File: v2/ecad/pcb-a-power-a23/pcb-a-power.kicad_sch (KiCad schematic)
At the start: 392 parts, among them Q1 2N7002: panel controller high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, Q10 CSD18510Q5B 40 V N-FET, Q11 CSD18510Q5B 40 V N-FET, Q12 CSD18510Q5B 40 V N-FET, Q13 CSD18510Q5B 40 V N-FET, Q14 CSD18510Q5B 40 V N-FET, Q15 CSD18510Q5B 40 V N-FET, Q16 CSD18510Q5B 40 V N-FET, Q17 CSD19532Q5B 100 V N-FET (4.6 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, Q18 CSD19532Q5B 100 V N-FET (4.6 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, Q19 CSD19532Q5B 100 V N-FET (4.6 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, Q2 CSD19532Q5B 100 V N-FET (4.6 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, Q20 CSD19532Q5B 100 V N-FET (4.6 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, Q21 CSD18510Q5B 40 V N-FET, Q22 CSD18510Q5B 40 V N-FET, Q23 CSD18510Q5B 40 V N-FET, Q24 CSD18510Q5B 40 V N-FET, Q25 CSD18510Q5B 40 V N-FET, Q26 CSD18510Q5B 40 V N-FET, Q27 CSD18510Q5B 40 V N-FET (VBUS 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, Q3 CSD19532Q5B 100 V N-FET (4.6 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, Q4 CSD19532Q5B 100 V N-FET (4.6 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, Q5 CSD19532Q5B 100 V N-FET (4.6 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, Q6 2N7002: CHG_INHIBIT high = IL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, Q7 CSD18510Q5B 40 V N-FET, Q8 CSD18510Q5B 40 V N-FET, Q9 CSD18510Q5B 40 V N-FET, U1 LTC2954CTS8-1 push-button on/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, U10 INA226 rail monitor +5V_S3, U11 INA226 rail monitor +5V_DEV, U12 TPS62933DRLR 3 A buck, 3.3 V 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, U13 LM5176PWPR buck-boost control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, U14 INA226 PA rail monitor (0x46), U15 LM5176PWPR buck-boost control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, U16 LM5176PWPR buck-boost control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, U17 INA226 PoE rail monitor (0x47), U18 TPS25740ARGER USB-C PD source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, U19 LM5176PWPR buck-boost control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, U2 LM5176PWPR buck-boost control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, U21 TPS259631DDAR eFuse VBAT -> V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, U22 TPS259631DDAR eFuse VBAT -> V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, U23 TPS259631DDAR eFuse +5V_DEV -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, U26 SN74LVC08APWR quad AND: EMCON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, U27 PCA9555PW (0x21): enables and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, U28 PCA9555PW (0x24): power-good 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, U29 USBLC6-2SC6, U3 BQ25731RSNR 1 to 5 cell buck-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, U4 AP64500SP-13 5 A buck, 5.1 V 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, U5 AP64500SP-13 5 A buck, 5.1 V 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, U6 AP64500SP-13 5 A buck, 5.1 V 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, U7 AP64500SP-13 5 A buck, 5.1 V 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, U8 INA226 rail monitor +5V_S1, U9 INA226 rail monitor +5V_S2

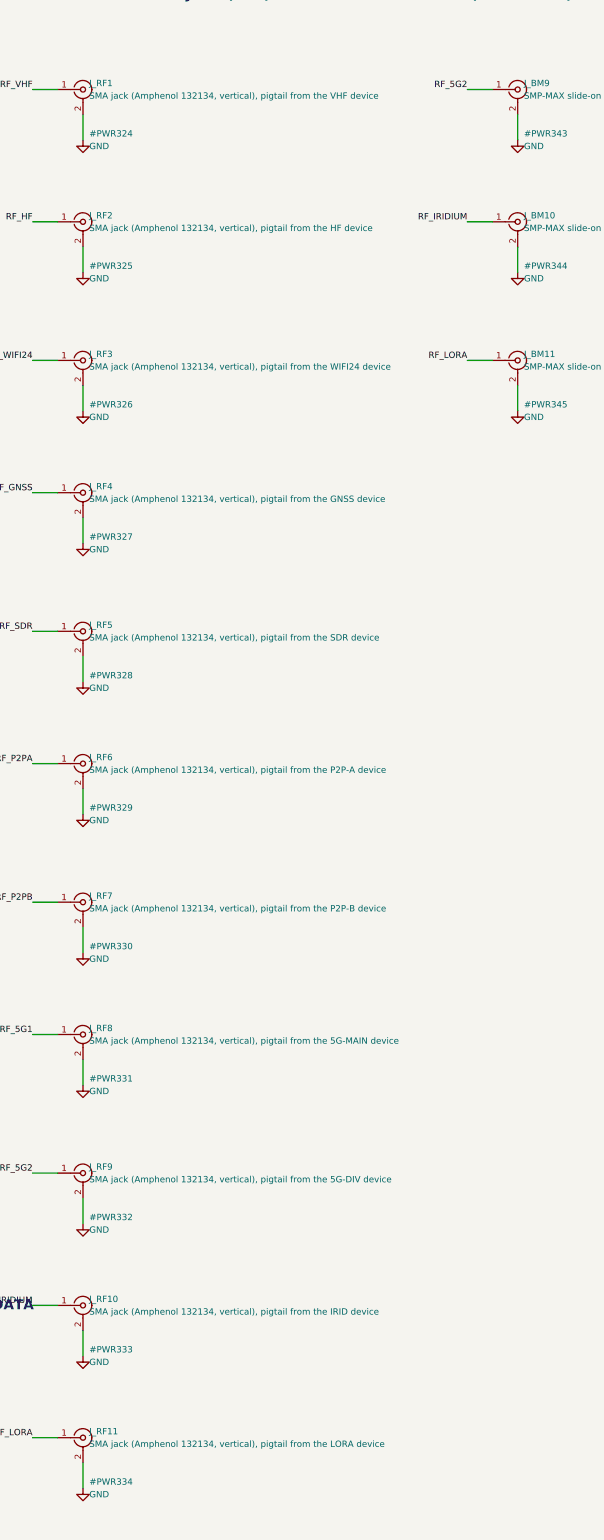
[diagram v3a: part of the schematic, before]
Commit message: feat(pcb-a,pcb-e): A24 re-cut and E7 cut, and boards A and E certify PASS [MESHSAT-862]
E7: routeflow ended CLEAN. hard 0, unrouted 0, check_pcb_e 88 of 88, dc_drop 2 of 2 rails MET,
netlist_board 816 of 816 with 18 aliased pins, verify_deliverable ALL PASS on 35 of 35, board sha256
b54cec80 matching the deliverable's own record. It carries today's connector corrections: the JST-VH
inlet and panel rows on C274411, the XT60-M pack connector on C98733, and the LT8705A's QFN order code
in place of the TSSOP one.

A24 re-cut with the SMA rows naming the jack instead of the radio at the far end of the pigtail. Same
board, same copper, one more text pass.

jlc_certify on the two of them: 223 components, 194 CERTIFIED, 23 HAND_FIT each with a written purchase
route, 6 BENCH_FITTED, NOTHING OPEN. It is the first PASS the certifier has returned on any board since
it was written on 11 September.
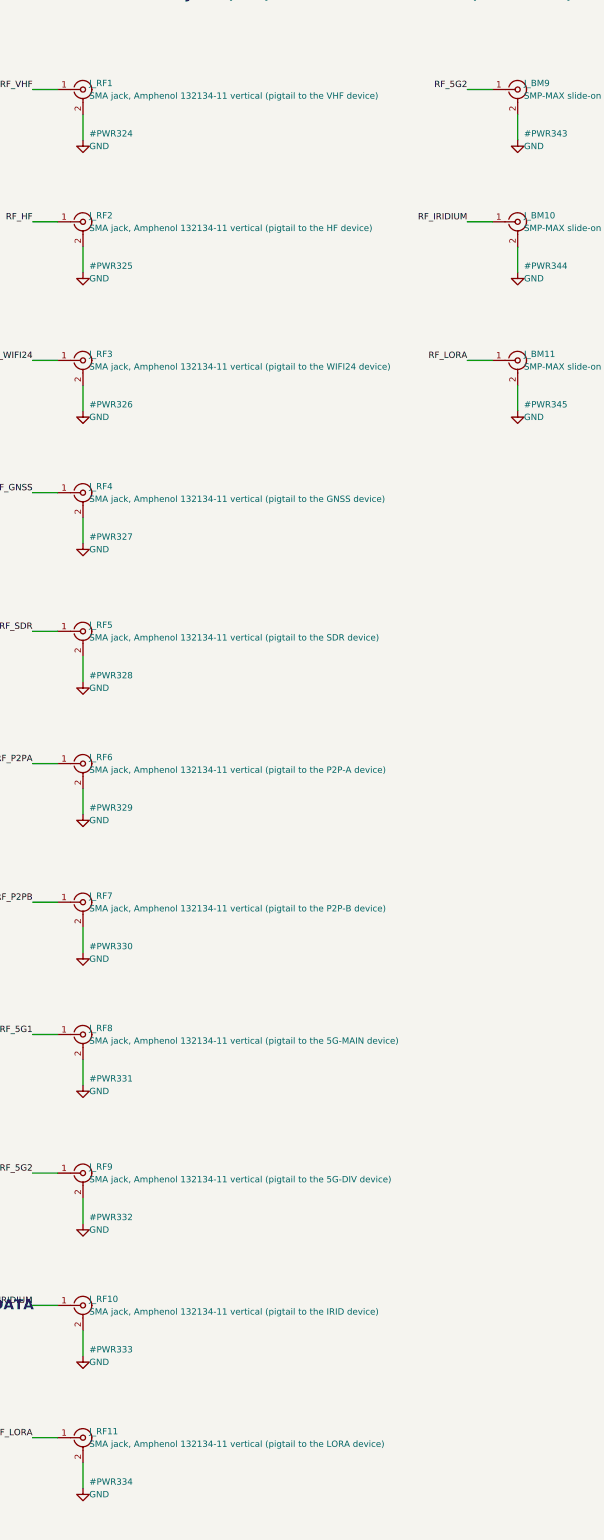
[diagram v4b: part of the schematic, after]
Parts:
- J_RF1: value SMA jack (Amphenol 132134, vertical), pigtail from the VHF device -> SMA jack, Amphenol 132134-11 vertical (pigtail to the VHF device)
- J_RF10: value SMA jack (Amphenol 132134, vertical), pigtail from the IRID device -> SMA jack, Amphenol 132134-11 vertical (pigtail to the IRID device)
- J_RF11: value SMA jack (Amphenol 132134, vertical), pigtail from the LORA device -> SMA jack, Amphenol 132134-11 vertical (pigtail to the LORA device)
- J_RF2: value SMA jack (Amphenol 132134, vertical), pigtail from the HF device -> SMA jack, Amphenol 132134-11 vertical (pigtail to the HF device)
- J_RF3: value SMA jack (Amphenol 132134, vertical), pigtail from the WIFI24 device -> SMA jack, Amphenol 132134-11 vertical (pigtail to the WIFI24 device)
- J_RF4: value SMA jack (Amphenol 132134, vertical), pigtail from the GNSS device -> SMA jack, Amphenol 132134-11 vertical (pigtail to the GNSS device)
- J_RF5: value SMA jack (Amphenol 132134, vertical), pigtail from the SDR device -> SMA jack, Amphenol 132134-11 vertical (pigtail to the SDR device)
- J_RF6: value SMA jack (Amphenol 132134, vertical), pigtail from the P2P-A device -> SMA jack, Amphenol 132134-11 vertical (pigtail to the P2P-A device)
- J_RF7: value SMA jack (Amphenol 132134, vertical), pigtail from the P2P-B device -> SMA jack, Amphenol 132134-11 vertical (pigtail to the P2P-B device)
- J_RF8: value SMA jack (Amphenol 132134, vertical), pigtail from the 5G-MAIN device -> SMA jack, Amphenol 132134-11 vertical (pigtail to the 5G-MAIN device)
- J_RF9: value SMA jack (Amphenol 132134, vertical), pigtail from the 5G-DIV device -> SMA jack, Amphenol 132134-11 vertical (pigtail to the 5G-DIV device)
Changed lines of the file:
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@@
 	(symbol (lib_id "Connector:Conn_Coaxial") (at 2504.44 43.18 0) (unit 1) (exclude_from_sim no) (in_bom yes) (on_board yes) (dnp no) (fields_autoplaced yes)
 		(property "Reference" "J_RF1" (at 2505.71 41.91 0) (effects (font (size 1.27 1.27)) (justify left)))
-		(property "Value" "SMA jack (Amphenol 132134, vertical), pigtail from the VHF device" (at 2505.71 44.45 0) (effects (font (size 1.27 1.27)) (justify left)))
+		(property "Value" "SMA jack, Amphenol 132134-11 vertical (pigtail to the VHF device)" (at 2505.71 44.45 0) (effects (font (size 1.27 1.27)) (justify left)))
 		(property "Footprint" "Connector_Coaxial:SMA_Amphenol_132134-11_Vertical" (at 2504.44 43.18 0) (effects (font (size 1.27 1.27)) (justify left) (hide yes)))
 		(property "Datasheet" "" (at 2504.44 43.18 0) (effects (font (size 1.27 1.27)) (justify left) (hide yes)))
@@
 	(symbol (lib_id "Connector:Conn_Coaxial") (at 2504.44 69.85 0) (unit 1) (exclude_from_sim no) (in_bom yes) (on_board yes) (dnp no) (fields_autoplaced yes)
 		(property "Reference" "J_RF2" (at 2505.71 68.58 0) (effects (font (size 1.27 1.27)) (justify left)))
-		(property "Value" "SMA jack (Amphenol 132134, vertical), pigtail from the HF device" (at 2505.71 71.12 0) (effects (font (size 1.27 1.27)) (justify left)))
+		(property "Value" "SMA jack, Amphenol 132134-11 vertical (pigtail to the HF device)" (at 2505.71 71.12 0) (effects (font (size 1.27 1.27)) (justify left)))
 		(property "Footprint" "Connector_Coaxial:SMA_Amphenol_132134-11_Vertical" (at 2504.44 69.85 0) (effects (font (size 1.27 1.27)) (justify left) (hide yes)))
 		(property "Datasheet" "" (at 2504.44 69.85 0) (effects (font (size 1.27 1.27)) (justify left) (hide yes)))
@@
 	(symbol (lib_id "Connector:Conn_Coaxial") (at 2504.44 97.79 0) (unit 1) (exclude_from_sim no) (in_bom yes) (on_board yes) (dnp no) (fields_autoplaced yes)
 		(property "Reference" "J_RF3" (at 2505.71 96.52 0) (effects (font (size 1.27 1.27)) (justify left)))
-		(property "Value" "SMA jack (Amphenol 132134, vertical), pigtail from the WIFI24 device" (at 2505.71 99.06 0) (effects (font (size 1.27 1.27)) (justify left)))
+		(property "Value" "SMA jack, Amphenol 132134-11 vertical (pigtail to the WIFI24 device)" (at 2505.71 99.06 0) (effects (font (size 1.27 1.27)) (justify left)))
 		(property "Footprint" "Connector_Coaxial:SMA_Amphenol_132134-11_Vertical" (at 2504.44 97.79 0) (effects (font (size 1.27 1.27)) (justify left) (hide yes)))
 		(property "Datasheet" "" (at 2504.44 97.79 0) (effects (font (size 1.27 1.27)) (justify left) (hide yes)))
@@
 	(symbol (lib_id "Connector:Conn_Coaxial") (at 2504.44 124.46 0) (unit 1) (exclude_from_sim no) (in_bom yes) (on_board yes) (dnp no) (fields_autoplaced yes)
 		(property "Reference" "J_RF4" (at 2505.71 123.19 0) (effects (font (size 1.27 1.27)) (justify left)))
-		(property "Value" "SMA jack (Amphenol 132134, vertical), pigtail from the GNSS device" (at 2505.71 125.73 0) (effects (font (size 1.27 1.27)) (justify left)))
+		(property "Value" "SMA jack, Amphenol 132134-11 vertical (pigtail to the GNSS device)" (at 2505.71 125.73 0) (effects (font (size 1.27 1.27)) (justify left)))
 		(property "Footprint" "Connector_Coaxial:SMA_Amphenol_132134-11_Vertical" (at 2504.44 124.46 0) (effects (font (size 1.27 1.27)) (justify left) (hide yes)))
 		(property "Datasheet" "" (at 2504.44 124.46 0) (effects (font (size 1.27 1.27)) (justify left) (hide yes)))
@@
 	(symbol (lib_id "Connector:Conn_Coaxial") (at 2504.44 152.40 0) (unit 1) (exclude_from_sim no) (in_bom yes) (on_board yes) (dnp no) (fields_autoplaced yes)
 		(property "Reference" "J_RF5" (at 2505.71 151.13 0) (effects (font (size 1.27 1.27)) (justify left)))
-		(property "Value" "SMA jack (Amphenol 132134, vertical), pigtail from the SDR device" (at 2505.71 153.67 0) (effects (font (size 1.27 1.27)) (justify left)))
+		(property "Value" "SMA jack, Amphenol 132134-11 vertical (pigtail to the SDR device)" (at 2505.71 153.67 0) (effects (font (size 1.27 1.27)) (justify left)))
 		(property "Footprint" "Connector_Coaxial:SMA_Amphenol_132134-11_Vertical" (at 2504.44 152.40 0) (effects (font (size 1.27 1.27)) (justify left) (hide yes)))
 		(property "Datasheet" "" (at 2504.44 152.40 0) (effects (font (size 1.27 1.27)) (justify left) (hide yes)))
@@
 	(symbol (lib_id "Connector:Conn_Coaxial") (at 2504.44 179.07 0) (unit 1) (exclude_from_sim no) (in_bom yes) (on_board yes) (dnp no) (fields_autoplaced yes)
 		(property "Reference" "J_RF6" (at 2505.71 177.80 0) (effects (font (size 1.27 1.27)) (justify left)))
-		(property "Value" "SMA jack (Amphenol 132134, vertical), pigtail from the P2P-A device" (at 2505.71 180.34 0) (effects (font (size 1.27 1.27)) (justify left)))
+		(property "Value" "SMA jack, Amphenol 132134-11 vertical (pigtail to the P2P-A device)" (at 2505.71 180.34 0) (effects (font (size 1.27 1.27)) (justify left)))
 		(property "Footprint" "Connector_Coaxial:SMA_Amphenol_132134-11_Vertical" (at 2504.44 179.07 0) (effects (font (size 1.27 1.27)) (justify left) (hide yes)))
 		(property "Datasheet" "" (at 2504.44 179.07 0) (effects (font (size 1.27 1.27)) (justify left) (hide yes)))
@@
 	(symbol (lib_id "Connector:Conn_Coaxial") (at 2504.44 207.01 0) (unit 1) (exclude_from_sim no) (in_bom yes) (on_board yes) (dnp no) (fields_autoplaced yes)
 		(property "Reference" "J_RF7" (at 2505.71 205.74 0) (effects (font (size 1.27 1.27)) (justify left)))
-		(property "Value" "SMA jack (Amphenol 132134, vertical), pigtail from the P2P-B device" (at 2505.71 208.28 0) (effects (font (size 1.27 1.27)) (justify left)))
+		(property "Value" "SMA jack, Amphenol 132134-11 vertical (pigtail to the P2P-B device)" (at 2505.71 208.28 0) (effects (font (size 1.27 1.27)) (justify left)))
 		(property "Footprint" "Connector_Coaxial:SMA_Amphenol_132134-11_Vertical" (at 2504.44 207.01 0) (effects (font (size 1.27 1.27)) (justify left) (hide yes)))
 		(property "Datasheet" "" (at 2504.44 207.01 0) (effects (font (size 1.27 1.27)) (justify left) (hide yes)))
@@
 	(symbol (lib_id "Connector:Conn_Coaxial") (at 2504.44 233.68 0) (unit 1) (exclude_from_sim no) (in_bom yes) (on_board yes) (dnp no) (fields_autoplaced yes)
 		(property "Reference" "J_RF8" (at 2505.71 232.41 0) (effects (font (size 1.27 1.27)) (justify left)))
-		(property "Value" "SMA jack (Amphenol 132134, vertical), pigtail from the 5G-MAIN device" (at 2505.71 234.95 0) (effects (font (size 1.27 1.27)) (justify left)))
+		(property "Value" "SMA jack, Amphenol 132134-11 vertical (pigtail to the 5G-MAIN device)" (at 2505.71 234.95 0) (effects (font (size 1.27 1.27)) (justify left)))
 		(property "Footprint" "Connector_Coaxial:SMA_Amphenol_132134-11_Vertical" (at 2504.44 233.68 0) (effects (font (size 1.27 1.27)) (justify left) (hide yes)))
 		(property "Datasheet" "" (at 2504.44 233.68 0) (effects (font (size 1.27 1.27)) (justify left) (hide yes)))
@@
 	(symbol (lib_id "Connector:Conn_Coaxial") (at 2504.44 261.62 0) (unit 1) (exclude_from_sim no) (in_bom yes) (on_board yes) (dnp no) (fields_autoplaced yes)
 		(property "Reference" "J_RF9" (at 2505.71 260.35 0) (effects (font (size 1.27 1.27)) (justify left)))
-		(property "Value" "SMA jack (Amphenol 132134, vertical), pigtail from the 5G-DIV device" (at 2505.71 262.89 0) (effects (font (size 1.27 1.27)) (justify left)))
+		(property "Value" "SMA jack, Amphenol 132134-11 vertical (pigtail to the 5G-DIV device)" (at 2505.71 262.89 0) (effects (font (size 1.27 1.27)) (justify left)))
 		(property "Footprint" "Connector_Coaxial:SMA_Amphenol_132134-11_Vertical" (at 2504.44 261.62 0) (effects (font (size 1.27 1.27)) (justify left) (hide yes)))
 		(property "Datasheet" "" (at 2504.44 261.62 0) (effects (font (size 1.27 1.27)) (justify left) (hide yes)))
@@
 	(symbol (lib_id "Connector:Conn_Coaxial") (at 2504.44 288.29 0) (unit 1) (exclude_from_sim no) (in_bom yes) (on_board yes) (dnp no) (fields_autoplaced yes)
 		(property "Reference" "J_RF10" (at 2505.71 287.02 0) (effects (font (size 1.27 1.27)) (justify left)))
-		(property "Value" "SMA jack (Amphenol 132134, vertical), pigtail from the IRID device" (at 2505.71 289.56 0) (effects (font (size 1.27 1.27)) (justify left)))
+		(property "Value" "SMA jack, Amphenol 132134-11 vertical (pigtail to the IRID device)" (at 2505.71 289.56 0) (effects (font (size 1.27 1.27)) (justify left)))
 		(property "Footprint" "Connector_Coaxial:SMA_Amphenol_132134-11_Vertical" (at 2504.44 288.29 0) (effects (font (size 1.27 1.27)) (justify left) (hide yes)))
 		(property "Datasheet" "" (at 2504.44 288.29 0) (effects (font (size 1.27 1.27)) (justify left) (hide yes)))
@@
 	(symbol (lib_id "Connector:Conn_Coaxial") (at 2504.44 314.96 0) (unit 1) (exclude_from_sim no) (in_bom yes) (on_board yes) (dnp no) (fields_autoplaced yes)
 		(property "Reference" "J_RF11" (at 2505.71 313.69 0) (effects (font (size 1.27 1.27)) (justify left)))
-		(property "Value" "SMA jack (Amphenol 132134, vertical), pigtail from the LORA device" (at 2505.71 316.23 0) (effects (font (size 1.27 1.27)) (justify left)))
+		(property "Value" "SMA jack, Amphenol 132134-11 vertical (pigtail to the LORA device)" (at 2505.71 316.23 0) (effects (font (size 1.27 1.27)) (justify left)))
 		(property "Footprint" "Connector_Coaxial:SMA_Amphenol_132134-11_Vertical" (at 2504.44 314.96 0) (effects (font (size 1.27 1.27)) (justify left) (hide yes)))
 		(property "Datasheet" "" (at 2504.44 314.96 0) (effects (font (size 1.27 1.27)) (justify left) (hide yes)))

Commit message: fix(sch): the six schematics regenerated on pages that hold them (A 2074 x 1230 mm in two bands, B 2074 x 1710); every netlist identical to the committed one apart from its source path [MESHSAT-862]
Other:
- moved on the sheet: C100, C101, C102, C103, C104, C106, C107, C98, C99, J_AB1, J_AB2, J_BM1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

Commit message: feat(ecad): readable schematics: a page engine draws every board as wired A3 pages of functional blocks (ICs as boxes with rails top and grounds bottom, passives on the pins they serve, decoupling rows, power symbols), proves the drawing's connectivity before writing, and the build cuts the sheet into A3 pages; all six netlists identical; the render scene puts the lit display on the glass and the monitor's rear block under it [MESHSAT-862]
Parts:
- removed C119, C14, C74: 10u 50V X7R 1210, Capacitor_SMD:C_1210_3225Metric, symbol Device:C
- removed C19, C4: 1u, Capacitor_SMD:C_0603_1608Metric, symbol Device:C
- removed C31: 22u 10V X7R 1210, Capacitor_SMD:C_1210_3225Metric, symbol Device:C
- removed C47: 10u 25V 1210, Capacitor_SMD:C_1210_3225Metric, symbol Device:C
- removed C60, C8: 4.7u, Capacitor_SMD:C_0805_2012Metric, symbol Device:C
- removed C84: 10u 100V X7R 1210, Capacitor_SMD:C_1210_3225Metric, symbol Device:C
- removed C87: 100p, Capacitor_SMD:C_0603_1608Metric, symbol Device:C
- removed C9: 100n 25V, Capacitor_SMD:C_0603_1608Metric, symbol Device:C
- removed J_HEAT: JST-XH 1x2 socket: the heater mat under the 2590 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, Connector_JST:JST_XH_B2B-XH-A_1x02_P2.50mm_Vertical, symbol Connector_Generic:Conn_01x02
- removed L11: 6.8uH XAL1010-682ME, Inductor_SMD:L_Coilcraft_XAL1010-XXX, symbol Device:L
- removed L4: 4.7uH XAL6060-472ME (Isat 11 A), Inductor_SMD:L_Coilcraft_XAL6060-XXX, symbol Device:L
- removed Q11, Q12, Q13, Q14, Q16, Q21, Q22, Q23, Q24, Q25, Q26, Q7, Q8, Q9: CSD18510Q5B 40 V N-FET, Package_SO:PowerPAK_SO-8_Single, symbol Connector_Generic:Conn_01x05
- removed Q17, Q18, Q19, Q2, Q20: CSD19532Q5B 100 V N-FET (4.6 mOhm at VGS 6 V, Pow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, Package_SO:PowerPAK_SO-8_Single, symbol Connector_Generic:Conn_01x05
- removed Q27: CSD18510Q5B 40 V N-FET (VBUS switch), Package_SO:PowerPAK_SO-8_Single, symbol Connector_Generic:Conn_01x05
- removed R110: 10k, Resistor_SMD:R_0603_1608Metric, symbol Device:R
- removed R27: 40.2k 1%, Resistor_SMD:R_0603_1608Metric, symbol Device:R
- removed R41: 10k 1%, Resistor_SMD:R_0603_1608Metric, symbol Device:R
- removed R42: 100k, Resistor_SMD:R_0603_1608Metric, symbol Device:R
- removed R6: 240k 1%, Resistor_SMD:R_0603_1608Metric, symbol Device:R
- removed U1: LTC2954CTS8-1 push-button on/off controller, Package_TO_SOT_SMD:TSOT-23-8, symbol Connector_Generic:Conn_01x08
- removed U10: INA226 rail monitor +5V_S3, Package_SO:VSSOP-10_3x3mm_P0.5mm, symbol Connector_Generic:Conn_01x10
- removed U11: INA226 rail monitor +5V_DEV, Package_SO:VSSOP-10_3x3mm_P0.5mm, symbol Connector_Generic:Conn_01x10
- removed U12: TPS62933DRLR 3 A buck, 3.3 V logic, Package_TO_SOT_SMD:SOT-583-8, symbol Connector_Generic:Conn_01x08
- removed U13: LM5176PWPR buck-boost controller, +13V8_PA from V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, Package_SO:HTSSOP-28-1EP_4.4x9.7mm_P0.65mm_EP2.85x5.4mm, symbol Connector_Generic:Conn_01x29
- removed U14: INA226 PA rail monitor (0x46), Package_SO:VSSOP-10_3x3mm_P0.5mm, symbol Connector_Generic:Conn_01x10
- removed U15: LM5176PWPR buck-boost controller, +12V_HF from VB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, Package_SO:HTSSOP-28-1EP_4.4x9.7mm_P0.65mm_EP2.85x5.4mm, symbol Connector_Generic:Conn_01x29
- removed U16: LM5176PWPR buck-boost controller, +54V_POE from V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, Package_SO:HTSSOP-28-1EP_4.4x9.7mm_P0.65mm_EP2.85x5.4mm, symbol Connector_Generic:Conn_01x29
- removed U17: INA226 PoE rail monitor (0x47), Package_SO:VSSOP-10_3x3mm_P0.5mm, symbol Connector_Generic:Conn_01x10
- removed U18: TPS25740ARGER USB-C PD source controller, 45 W ou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, Package_DFN_QFN:QFN-24-1EP_4x4mm_P0.5mm_EP2.5x2.5mm, symbol Connector_Generic:Conn_01x25
- removed U19: LM5176PWPR buck-boost controller, PD_VPWR from VB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, Package_SO:HTSSOP-28-1EP_4.4x9.7mm_P0.65mm_EP2.85x5.4mm, symbol Connector_Generic:Conn_01x29
- removed U2: LM5176PWPR buck-boost controller, VBUS20 from VIN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, Package_SO:HTSSOP-28-1EP_4.4x9.7mm_P0.65mm_EP2.85x5.4mm, symbol Connector_Generic:Conn_01x29
- removed U21: TPS259631DDAR eFuse VBAT -> VMON (750R 1% (ILM: 1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, Package_SO:SOIC-8-1EP_3.9x4.9mm_P1.27mm_EP2.29x3mm, symbol Connector_Generic:Conn_01x09
- removed U22: TPS259631DDAR eFuse VBAT -> VHEAT (909R 1% (ILM: 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, Package_SO:SOIC-8-1EP_3.9x4.9mm_P1.27mm_EP2.29x3mm, symbol Connector_Generic:Conn_01x09
- removed U23: TPS259631DDAR eFuse +5V_DEV -> +5V_D8 (453R 1% (I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, Package_SO:SOIC-8-1EP_3.9x4.9mm_P1.27mm_EP2.29x3mm, symbol Connector_Generic:Conn_01x09
- removed U26: SN74LVC08APWR quad AND: EMCON gates for the PA ra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, Package_SO:TSSOP-14_4.4x5mm_P0.65mm, symbol Connector_Generic:Conn_01x14
- removed U27: PCA9555PW (0x21): enables and status, Package_SO:TSSOP-24_4.4x7.8mm_P0.65mm, symbol Interface_Expansion:PCA9555PW
- removed U3: BQ25731RSNR 1 to 5 cell buck-boost charger, 4S fr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, Package_DFN_QFN:QFN-32-1EP_4x4mm_P0.4mm_EP2.65x2.65mm, symbol Connector_Generic:Conn_01x33
- removed U4: AP64500SP-13 5 A buck, 5.1 V rail +5V_S1, Package_SO:SOIC-8-1EP_3.9x4.9mm_P1.27mm_EP2.29x3mm, symbol Connector_Generic:Conn_01x09
- removed U5: AP64500SP-13 5 A buck, 5.1 V rail +5V_S2, Package_SO:SOIC-8-1EP_3.9x4.9mm_P1.27mm_EP2.29x3mm, symbol Connector_Generic:Conn_01x09
- removed U6: AP64500SP-13 5 A buck, 5.1 V rail +5V_S3, Package_SO:SOIC-8-1EP_3.9x4.9mm_P1.27mm_EP2.29x3mm, symbol Connector_Generic:Conn_01x09
- removed U7: AP64500SP-13 5 A buck, 5.1 V rail +5V_DEV, Package_SO:SOIC-8-1EP_3.9x4.9mm_P1.27mm_EP2.29x3mm, symbol Connector_Generic:Conn_01x09
- removed U8: INA226 rail monitor +5V_S1, Package_SO:VSSOP-10_3x3mm_P0.5mm, symbol Connector_Generic:Conn_01x10
- removed U9: INA226 rail monitor +5V_S2, Package_SO:VSSOP-10_3x3mm_P0.5mm, symbol Connector_Generic:Conn_01x10
- added C100, C53, C86: 10n, Capacitor_SMD:C_0603_1608Metric, symbol Device:C
- added C11: 10u 50V X7R 1210, Capacitor_SMD:C_1210_3225Metric, symbol Device:C
- added C120: 10u 25V 1210, Capacitor_SMD:C_1210_3225Metric, symbol Device:C
- added C16, C91: 100n 25V, Capacitor_SMD:C_0603_1608Metric, symbol Device:C
- added C37, C56: 22u 10V X7R 1210, Capacitor_SMD:C_1210_3225Metric, symbol Device:C
- added C94: 220n, Capacitor_SMD:C_0603_1608Metric, symbol Device:C
- added J_5V_S2: slot 2 5.1 V rail to B16 (JST-VH, 16 AWG): + -, Connector_JST:JST_VH_B2P-VH_1x02_P3.96mm_Vertical, symbol Connector_Generic:Conn_01x02
- added J_RF1, J_RF7: SMA jack, Amphenol 132134-11 vertical (pigtail to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, Connector_Coaxial:SMA_Amphenol_132134-11_Vertical, symbol Connector:Conn_Coaxial
- added L7: 4.7uH XAL4030-472ME, Inductor_SMD:L_Coilcraft_XAL4030-XXX, symbol Device:L
- added L9: 6.8uH XAL1010-682ME, Inductor_SMD:L_Coilcraft_XAL1010-XXX, symbol Device:L
- added Q10: CSD18510Q5B 40 V N-FET, Package_SO:PowerPAK_SO-8_Single, symbol meshsat_ic:Q10
- added Q12: CSD18510Q5B 40 V N-FET, Package_SO:PowerPAK_SO-8_Single, symbol meshsat_ic:Q12
- added Q13: CSD18510Q5B 40 V N-FET, Package_SO:PowerPAK_SO-8_Single, symbol meshsat_ic:Q13
- added Q14: CSD18510Q5B 40 V N-FET, Package_SO:PowerPAK_SO-8_Single, symbol meshsat_ic:Q14
- added Q15: CSD18510Q5B 40 V N-FET, Package_SO:PowerPAK_SO-8_Single, symbol meshsat_ic:Q15
- added Q16: CSD18510Q5B 40 V N-FET, Package_SO:PowerPAK_SO-8_Single, symbol meshsat_ic:Q16
- added Q18: CSD19532Q5B 100 V N-FET (4.6 mOhm at VGS 6 V, Pow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, Package_SO:PowerPAK_SO-8_Single, symbol meshsat_ic:Q18
- added Q19: CSD19532Q5B 100 V N-FET (4.6 mOhm at VGS 6 V, Pow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, Package_SO:PowerPAK_SO-8_Single, symbol meshsat_ic:Q19
- added Q2: CSD19532Q5B 100 V N-FET (4.6 mOhm at VGS 6 V, Pow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, Package_SO:PowerPAK_SO-8_Single, symbol meshsat_ic:Q2
- added Q20: CSD19532Q5B 100 V N-FET (4.6 mOhm at VGS 6 V, Pow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, Package_SO:PowerPAK_SO-8_Single, symbol meshsat_ic:Q20
- added Q23: CSD18510Q5B 40 V N-FET, Package_SO:PowerPAK_SO-8_Single, symbol meshsat_ic:Q23
- added Q24: CSD18510Q5B 40 V N-FET, Package_SO:PowerPAK_SO-8_Single, symbol meshsat_ic:Q24
- added Q25: CSD18510Q5B 40 V N-FET, Package_SO:PowerPAK_SO-8_Single, symbol meshsat_ic:Q25
- added Q26: CSD18510Q5B 40 V N-FET, Package_SO:PowerPAK_SO-8_Single, symbol meshsat_ic:Q26
- added Q27: CSD18510Q5B 40 V N-FET (VBUS switch), Package_SO:PowerPAK_SO-8_Single, symbol meshsat_ic:Q27
- added Q3: CSD19532Q5B 100 V N-FET (4.6 mOhm at VGS 6 V, Pow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, Package_SO:PowerPAK_SO-8_Single, symbol meshsat_ic:Q3
- added Q4: CSD19532Q5B 100 V N-FET (4.6 mOhm at VGS 6 V, Pow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, Package_SO:PowerPAK_SO-8_Single, symbol meshsat_ic:Q4
- added Q5: CSD19532Q5B 100 V N-FET (4.6 mOhm at VGS 6 V, Pow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, Package_SO:PowerPAK_SO-8_Single, symbol meshsat_ic:Q5
- added Q7: CSD18510Q5B 40 V N-FET, Package_SO:PowerPAK_SO-8_Single, symbol meshsat_ic:Q7
- added Q8: CSD18510Q5B 40 V N-FET, Package_SO:PowerPAK_SO-8_Single, symbol meshsat_ic:Q8
- added Q9: CSD18510Q5B 40 V N-FET, Package_SO:PowerPAK_SO-8_Single, symbol meshsat_ic:Q9
- added R140: 1M (GD to VPWR, 9.1.3), Resistor_SMD:R_0603_1608Metric, symbol Device:R
- added R3: 100k, Resistor_SMD:R_0603_1608Metric, symbol Device:R
- added R68: 40.2k (300 kHz), Resistor_SMD:R_0603_1608Metric, symbol Device:R
- added R95: 10k, Resistor_SMD:R_0603_1608Metric, symbol Device:R
- added TP26: EXP2_SPD, TestPoint:TestPoint_Pad_D1.5mm, symbol Connector:TestPoint
- added U1: LTC2954CTS8-1 push-button on/off controller, Package_TO_SOT_SMD:TSOT-23-8, symbol meshsat_ic:U1
- added U10: INA226 rail monitor +5V_S3, Package_SO:VSSOP-10_3x3mm_P0.5mm, symbol meshsat_ic:U10
- added U11: INA226 rail monitor +5V_DEV, Package_SO:VSSOP-10_3x3mm_P0.5mm, symbol meshsat_ic:U11
- added U12: TPS62933DRLR 3 A buck, 3.3 V logic, Package_TO_SOT_SMD:SOT-583-8, symbol meshsat_ic:U12
- added U13: LM5176PWPR buck-boost controller, +13V8_PA from V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, Package_SO:HTSSOP-28-1EP_4.4x9.7mm_P0.65mm_EP2.85x5.4mm, symbol meshsat_ic:U13
- added U14: INA226 PA rail monitor (0x46), Package_SO:VSSOP-10_3x3mm_P0.5mm, symbol meshsat_ic:U14
- added U15: LM5176PWPR buck-boost controller, +12V_HF from VB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, Package_SO:HTSSOP-28-1EP_4.4x9.7mm_P0.65mm_EP2.85x5.4mm, symbol meshsat_ic:U15
- added U16: LM5176PWPR buck-boost controller, +54V_POE from V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, Package_SO:HTSSOP-28-1EP_4.4x9.7mm_P0.65mm_EP2.85x5.4mm, symbol meshsat_ic:U16
- added U17: INA226 PoE rail monitor (0x47), Package_SO:VSSOP-10_3x3mm_P0.5mm, symbol meshsat_ic:U17
- added U18: TPS25740ARGER USB-C PD source controller, 45 W ou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, Package_DFN_QFN:QFN-24-1EP_4x4mm_P0.5mm_EP2.5x2.5mm, symbol meshsat_ic:U18
- added U19: LM5176PWPR buck-boost controller, PD_VPWR from VB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, Package_SO:HTSSOP-28-1EP_4.4x9.7mm_P0.65mm_EP2.85x5.4mm, symbol meshsat_ic:U19
- added U2: LM5176PWPR buck-boost controller, VBUS20 from VIN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, Package_SO:HTSSOP-28-1EP_4.4x9.7mm_P0.65mm_EP2.85x5.4mm, symbol meshsat_ic:U2
- added U21: TPS259631DDAR eFuse VBAT -> VMON (750R 1% (ILM: 1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, Package_SO:SOIC-8-1EP_3.9x4.9mm_P1.27mm_EP2.29x3mm, symbol meshsat_ic:U21
- added U22: TPS259631DDAR eFuse VBAT -> VHEAT (909R 1% (ILM: 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, Package_SO:SOIC-8-1EP_3.9x4.9mm_P1.27mm_EP2.29x3mm, symbol meshsat_ic:U22
- added U23: TPS259631DDAR eFuse +5V_DEV -> +5V_D8 (453R 1% (I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, Package_SO:SOIC-8-1EP_3.9x4.9mm_P1.27mm_EP2.29x3mm, symbol meshsat_ic:U23
- added U26: SN74LVC08APWR quad AND: EMCON gates for the PA ra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, Package_SO:TSSOP-14_4.4x5mm_P0.65mm, symbol meshsat_ic:U26
- added U3: BQ25731RSNR 1 to 5 cell buck-boost charger, 4S fr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, Package_DFN_QFN:QFN-32-1EP_4x4mm_P0.4mm_EP2.65x2.65mm, symbol meshsat_ic:U3
- added U4: AP64500SP-13 5 A buck, 5.1 V rail +5V_S1, Package_SO:SOIC-8-1EP_3.9x4.9mm_P1.27mm_EP2.29x3mm, symbol meshsat_ic:U4
- added U5: AP64500SP-13 5 A buck, 5.1 V rail +5V_S2, Package_SO:SOIC-8-1EP_3.9x4.9mm_P1.27mm_EP2.29x3mm, symbol meshsat_ic:U5
- added U6: AP64500SP-13 5 A buck, 5.1 V rail +5V_S3, Package_SO:SOIC-8-1EP_3.9x4.9mm_P1.27mm_EP2.29x3mm, symbol meshsat_ic:U6
- added U7: AP64500SP-13 5 A buck, 5.1 V rail +5V_DEV, Package_SO:SOIC-8-1EP_3.9x4.9mm_P1.27mm_EP2.29x3mm, symbol meshsat_ic:U7
- added U8: INA226 rail monitor +5V_S1, Package_SO:VSSOP-10_3x3mm_P0.5mm, symbol meshsat_ic:U8
- added U9: INA226 rail monitor +5V_S2, Package_SO:VSSOP-10_3x3mm_P0.5mm, symbol meshsat_ic:U9
- C119: renamed from C94; value 220n -> 10u 50V X7R 1210; footprint Capacitor_SMD:C_0603_1608Metric -> Capacitor_SMD:C_1210_3225Metric
- C19: renamed from Q10; value CSD18510Q5B 40 V N-FET -> 1u; footprint Package_SO:PowerPAK_SO-8_Single -> Capacitor_SMD:C_0603_1608Metric; symbol Connector_Generic:Conn_01x05 -> Device:C
- C4: renamed from R3; value 100k -> 1u; footprint Resistor_SMD:R_0603_1608Metric -> Capacitor_SMD:C_0603_1608Metric; symbol Device:R -> Device:C
- C47: renamed from C56; value 22u 10V X7R 1210 -> 10u 25V 1210
- C60: renamed from Q15; value CSD18510Q5B 40 V N-FET -> 4.7u; footprint Package_SO:PowerPAK_SO-8_Single -> Capacitor_SMD:C_0805_2012Metric; symbol Connector_Generic:Conn_01x05 -> Device:C
- C74: renamed from R68; value 40.2k (300 kHz) -> 10u 50V X7R 1210; footprint Resistor_SMD:R_0603_1608Metric -> Capacitor_SMD:C_1210_3225Metric; symbol Device:R -> Device:C
- C8: renamed from R12; value 5mOhm 1% 2512 (CS) -> 4.7u; footprint Resistor_SMD:R_2512_6332Metric -> Capacitor_SMD:C_0805_2012Metric; symbol Device:R -> Device:C
- C84: renamed from C86; value 10n -> 10u 100V X7R 1210; footprint Capacitor_SMD:C_0603_1608Metric -> Capacitor_SMD:C_1210_3225Metric
- C87: renamed from R140; value 1M (GD to VPWR, 9.1.3) -> 100p; footprint Resistor_SMD:R_0603_1608Metric -> Capacitor_SMD:C_0603_1608Metric; symbol Device:R -> Device:C
- C9: renamed from Q5; value CSD19532Q5B 100 V N-FET (4.6 mOhm at VGS 6 V, PowerPAK SO-8 / SON-8 5x6) -> 100n 25V; footprint Package_SO:PowerPAK_SO-8_Single -> Capacitor_SMD:C_0603_1608Metric; symbol Connector_Generic:Conn_01x05 -> Device:C; LCSC C473333 -> (none)
- J_HEAT: renamed from TP26; value EXP2_SPD -> JST-XH 1x2 socket: the heater mat under the 2590 cradle, + and -; footprint TestPoint:TestPoint_Pad_D1.5mm -> Connector_JST:JST_XH_B2B-XH-A_1x02_P2.50mm_Vertical; symbol Connector:TestPoint -> Connector_Generic:Conn_01x02; LCSC (none) -> C265283; now in the parts list
- L11: renamed from C120; value 10u 25V 1210 -> 6.8uH XAL1010-682ME; footprint Capacitor_SMD:C_1210_3225Metric -> Inductor_SMD:L_Coilcraft_XAL1010-XXX; symbol Device:C -> Device:L
- L4: renamed from J_5V_S2; value slot 2 5.1 V rail to B16 (JST-VH, 16 AWG): + - -> 4.7uH XAL6060-472ME (Isat 11 A); footprint Connector_JST:JST_VH_B2P-VH_1x02_P3.96mm_Vertical -> Inductor_SMD:L_Coilcraft_XAL6060-XXX; symbol Connector_Generic:Conn_01x02 -> Device:L; LCSC C274411 -> (none)
- Q11: renamed from L9; value 6.8uH XAL1010-682ME -> CSD18510Q5B 40 V N-FET; footprint Inductor_SMD:L_Coilcraft_XAL1010-XXX -> Package_SO:PowerPAK_SO-8_Single; symbol Device:L -> meshsat_ic:Q11
- Q17: renamed from C91; value 100n 25V -> CSD19532Q5B 100 V N-FET (4.6 mOhm at VGS 6 V, PowerPAK SO-8 / SON-8 5x6); footprint Capacitor_SMD:C_0603_1608Metric -> Package_SO:PowerPAK_SO-8_Single; symbol Device:C -> meshsat_ic:Q17; LCSC (none) -> C473333
- Q21: renamed from C100; value 10n -> CSD18510Q5B 40 V N-FET; footprint Capacitor_SMD:C_0603_1608Metric -> Package_SO:PowerPAK_SO-8_Single; symbol Device:C -> meshsat_ic:Q21
- Q22: renamed from R95; value 10k -> CSD18510Q5B 40 V N-FET; footprint Resistor_SMD:R_0603_1608Metric -> Package_SO:PowerPAK_SO-8_Single; symbol Device:R -> meshsat_ic:Q22
- R110: renamed from J_RF7; value SMA jack, Amphenol 132134-11 vertical (pigtail to the P2P-B device) -> 10k; footprint Connector_Coaxial:SMA_Amphenol_132134-11_Vertical -> Resistor_SMD:R_0603_1608Metric; symbol Connector:Conn_Coaxial -> Device:R; LCSC C3174425 -> (none)
- R12: renamed from Q4; value CSD19532Q5B 100 V N-FET (4.6 mOhm at VGS 6 V, PowerPAK SO-8 / SON-8 5x6) -> 5mOhm 1% 2512 (CS); footprint Package_SO:PowerPAK_SO-8_Single -> Resistor_SMD:R_2512_6332Metric; symbol Connector_Generic:Conn_01x05 -> Device:R; LCSC C473333 -> (none)
- R27: renamed from C16; value 100n 25V -> 40.2k 1%; footprint Capacitor_SMD:C_0603_1608Metric -> Resistor_SMD:R_0603_1608Metric; symbol Device:C -> Device:R
- R41: renamed from C53; value 10n -> 10k 1%; footprint Capacitor_SMD:C_0603_1608Metric -> Resistor_SMD:R_0603_1608Metric; symbol Device:C -> Device:R
- R42: renamed from L7; value 4.7uH XAL4030-472ME -> 100k; footprint Inductor_SMD:L_Coilcraft_XAL4030-XXX -> Resistor_SMD:R_0603_1608Metric; symbol Device:L -> Device:R
- R6: renamed from Q3; value CSD19532Q5B 100 V N-FET (4.6 mOhm at VGS 6 V, PowerPAK SO-8 / SON-8 5x6) -> 240k 1%; footprint Package_SO:PowerPAK_SO-8_Single -> Resistor_SMD:R_0603_1608Metric; symbol Connector_Generic:Conn_01x05 -> Device:R; LCSC C473333 -> (none)
- U27: renamed from J_RF1; value SMA jack, Amphenol 132134-11 vertical (pigtail to the VHF device) -> PCA9555PW (0x21): enables and status; footprint Connector_Coaxial:SMA_Amphenol_132134-11_Vertical -> Package_SO:TSSOP-24_4.4x7.8mm_P0.65mm; symbol Connector:Conn_Coaxial -> Interface_Expansion:PCA9555PW; LCSC C3174425 -> C2864778
- renumbered C11 to C14, C37 to C31
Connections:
- net +12V_HF: now also U15.12 (+12V_HF), U15.13 (+12V_HF), U15.24 (+12V_HF)
- net +13V8_PA: now also U13.12 (+13V8_PA), U13.13 (+13V8_PA), U13.24 (+13V8_PA), U14.8 (+13V8_PA), U14.9 (+13V8_PA)
- net +3V3: now also R110.2, U27.21 (A0), U27.24 (VDD), C56.1, L7.2, R3.2, R95.2, U10.1 (+3V3), U10.6 (+3V3), U11.1 (+3V3), U11.2 (+3V3), U11.6 (+3V3)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; no longer C4.2, C47.1, Q22.2, R42.2
- net +54V_POE: now also C84.1, U16.12 (+54V_POE), U16.13 (+54V_POE), U17.9 (+54V_POE)
- net +5V_D8: now also U23.5 (+5V_D8)
- net +5V_DEV: now also U11.8 (+5V_DEV), U11.9 (+5V_DEV), U18.17 (+5V_DEV), U23.4 (+5V_DEV)
- net +5V_S1: now also C31.1, U8.8 (+5V_S1), U8.9 (+5V_S1)
- net +5V_S2: now also C37.1, J_5V_S2.1 (Pin_1), U9.8 (+5V_S2), U9.9 (+5V_S2); no longer C31.1, L4.1 (Pin_1)
- net +5V_S3: now also U10.8 (+5V_S3), U10.9 (+5V_S3)
- net B33_BST: now also U12.6 (B33_BST)
- net B33_FB: now also U12.8 (B33_FB)
- net B33_SS: now also C53.1, U12.7 (B33_SS); no longer R41.1
- net B33_SW: now also L7.1, U12.5 (B33_SW); no longer R42.1
- net CELL+: now also U3.19 (CELL+)
- net CHG_ILIM: now also U3.6 (CHG_ILIM)
- net CHG_INHIBIT: now also U27.4 (IO0_0)
- net CHRG_OK: now also U27.13 (IO1_0), U3.4 (CHRG_OK)
- net CH_ACN: now also Q7.5 (CH_ACN), U3.2 (CH_ACN)
- net CH_BTST1: now also C16.1, U3.30 (CH_BTST1); no longer R27.1
- net CH_BTST2: now also U3.25 (CH_BTST2)
- net CH_CELL: now also R27.1, U3.18 (CH_CELL)
- net CH_COMP1: now also U3.16 (CH_COMP1)
- net CH_COMP2: now also U3.17 (CH_COMP2)
- net CH_HIDRV1: now also Q7.4 (CH_HIDRV1), U3.31 (CH_HIDRV1)
- net CH_HIDRV2: now also Q10.4 (CH_HIDRV2), U3.24 (CH_HIDRV2); no longer C19.4 (Pin_4)
- net CH_LODRV1: now also Q8.4 (CH_LODRV1), U3.29 (CH_LODRV1)
- net CH_LODRV2: now also Q9.4 (CH_LODRV2), U3.26 (CH_LODRV2)
- net CH_SRP: now also Q10.5 (CH_SRP), U3.20 (CH_SRP), U3.22 (CH_SRP); no longer C19.5 (Pin_5)
- net CH_SW1: now also C16.2, Q7.1 (CH_SW1), Q7.2 (CH_SW1), Q7.3 (CH_SW1), Q8.5 (CH_SW1), U3.32 (CH_SW1); no longer R27.2
- net CH_SW2: now also Q10.1 (CH_SW2), Q10.2 (CH_SW2), Q10.3 (CH_SW2), Q9.5 (CH_SW2), U3.23 (CH_SW2); no longer C19.1 (Pin_1), C19.2 (Pin_2), C19.3 (Pin_3)
- net CH_VDDA: now also C19.1, U3.7 (CH_VDDA)
- net D8_EN: now also U27.7 (IO0_3), U23.3 (D8_EN)
- net D8_FLT: now also U27.17 (IO1_4), U23.6 (D8_FLT)
- net DEV_EN: now also R42.1, U27.11 (IO0_7), U7.3 (DEV_EN)
- net DOCK_SPARE: now also U27.18 (IO1_5)
- net EMCON_HW: now also U26.1 (EMCON_HW), U26.4 (EMCON_HW)
- net EXP2_SPD: now also TP26.1; no longer J_HEAT.1
- net EXP_INT: now also R110.1, U27.1 (~{INT})
- net FE_BOOT1: now also C9.1, U2.26 (FE_BOOT1)
- net FE_BOOT2: now also U2.20 (FE_BOOT2)
- net FE_COMP: now also U2.9 (FE_COMP)
- net FE_CS: now also Q3.1 (FE_CS), Q3.2 (FE_CS), Q3.3 (FE_CS), Q4.1 (FE_CS), Q4.2 (FE_CS), Q4.3 (FE_CS), U2.16 (FE_CS); no longer C8.1, R12.2 (Pin_2), R12.3 (Pin_3), R6.1 (Pin_1), R6.2 (Pin_2), R6.3 (Pin_3)
- net FE_EN: now also U2.1 (FE_EN)
- net FE_FB: now also R6.2, U2.11 (FE_FB)
- net FE_HDRV1: now also Q2.4 (FE_HDRV1), U2.27 (FE_HDRV1)
- net FE_HDRV2: now also Q5.4 (FE_HDRV2), U2.19 (FE_HDRV2); no longer C9.4 (Pin_4)
- net FE_LDRV1: now also Q3.4 (FE_LDRV1), U2.25 (FE_LDRV1); no longer R6.4 (Pin_4)
- net FE_LDRV2: now also Q4.4 (FE_LDRV2), U2.21 (FE_LDRV2); no longer R12.4 (Pin_4)
- net FE_MODE: now also U2.4 (FE_MODE)
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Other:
- note added: "100k"
- note added: "10k"
- note added: "10k 1%"
- note added: "10mOhm 1%"
- note added: "10mOhm 1% 2512"
- note added: "10u 100V"
- note added: "10u 25V"
- note added: "10u 35V"
- note added: "10u 50V"
- note added: "10uH XAL1010-103ME"
- note added: "12.0 V to the QMX HF unit in its l.."
- note added: "13.8 V to the PA module on the fac.."
- note added: "14.0k 1%"
- note added: "1M"
- note added: "20k 1%"
- note added: "20mOhm 1% 2512"
- note added: "21.0k 1%"
- note added: "22u 10V"
- note added: "22uH XAL1010-223ME"
- note added: "25 A mini blade"
- note added: "2N7002"
- note added: "2mOhm 1% 2512"
- note added: "3.3uH XAL6030-332ME"
- note added: "30k"
- note added: "4.7uH"
- note added: "4.7uH XAL6060-472ME"
- note added: "40.2k"
- note added: "43R 1W 2512"
- note added: "453R 1%"
- note added: "54 V to the PoE injector on B16"
- note added: "5mOhm 1%"
- note added: "5mOhm 1% 2512"
- note added: "6.8uH XAL1010-682ME"
- note added: "60.4k 1%"
- note added: "68k"
- note added: "750R 1%"
- note added: "9 A spring pin"
- note added: "909R 1%"
- note added: "A-B interconnect"
- note added: "A-B wall-port ribbon"
- note added: "AP64500SP-13 5 A buck"
- note added: "BQ25731RSNR 1 to 5 cell buck-boost.."
- note added: "CSD18510Q5B 40 V N-FET"
- note added: "CSD19532Q5B 100 V N-FET"
- note added: "D8 mezzanine 5 V"
- note added: "D8 mezzanine harness"
- note added: "EFUSES | EMCON GATES 74LVC08, EXPANDERS 0x21 0x24"
- note added: "FRONT END | CHARGER BQ25731"
- note added: "FRONT END: LM5176 FROM THE 9 TO 36 V INPUT TO THE 20 V CHARGE BUS (continued)"
- note added: "HF RAIL"
- note added: "INA226 PA rail monitor"
- note added: "INA226 PoE rail monitor"
- note added: "JST-PH 1x4 socket"
- note added: "JST-XH 1x2 socket"
- note added: "LM5176PWPR buck-boost controller"
- note added: "LTC2954CTS8-1 push-button on/off c.."
- note added: "PA RAIL"
- note added: "PACK NODE OVER THE DOCK BLOCK (32.56) | MAIN POWER CONTROL LTC2954 | FRONT END"
- note added: "PCA9555PW"
- note added: "PCB-A POWER + I/O A34"
- note added: "POE RAIL"
- note added: "RIBBON J_AB1 2x13, WALL-PORT RIBBON J_AB2 2x5, MEZZANINE HARNESS J_MEZZ1 2x8, WALL USB DATA"
- note added: "RIBBON J_AB1 2x13, WALL-PORT RIBBON J_AB2 2x5, MEZZANINE HARNESS J_MEZZ1 2x8, WALL USB DATA | ELEVEN BLIND-MATE RF SITES | TEST POINTS, FLAGS"
- note added: "SLOT RAIL S1 | SLOT RAIL S2 | SLOT RAIL S3"
- note added: "SLOT RAIL S3 | DEVICE RAIL | 3.3 V LOGIC"
- note added: "SLOT RAIL S3: AP64500 5.1 V + INA226 0x44 (continued)"
- note added: "SMA jack"
- note added: "SMBJ18A"
- note added: "SMCJ18A"
- note added: "SMCJ33A"
- note added: "SMP-MAX slide-on receptacle R222M0.."
- note added: "SN74LVC08APWR quad AND"
- note added: "TEST POINTS, FLAGS (continued)"
- note added: "TPS25740ARGER USB-C PD source cont.."
- note added: "TPS259631DDAR eFuse +5V_DEV -> +5V.."
- note added: "TPS259631DDAR eFuse VBAT -> VHEAT"
- note added: "TPS259631DDAR eFuse VBAT -> VMON"
- note added: "TPS62933DRLR 3 A buck"
- note added: "USB device rail to B16"
- note added: "USB-C PD OUTLET"
- note added: "decoupling of U13"
- note added: "decoupling of U15"
- note added: "decoupling of U16"
- note added: "decoupling of U19"
- note added: "decoupling of U2"
- note added: "monitor supply lead to the Xenarc"
- note added: "page 1 of 11 MeshSat field kit V2, CERN-OHL-S-2.0 PROTOTYPE, nothing built 2026-09-15"
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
